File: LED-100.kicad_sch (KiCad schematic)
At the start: 98 parts, among them J2 LDA100_2_J2, J3 LDA100_2_J3, J4 LDA100_2_J4, J5 xtra, J6 Conn_01x09, J7 Conn_01x01, SW1 SW_SPDT, U1 TLC5947DAP, U2 TLC5947DAP, U3 TLC5947DAP

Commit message: cleanup
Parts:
- U4: value ~ -> TEENSY 4.0
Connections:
- net GND: now also R1.2, R2.2, R3.2; no longer R1.1, R2.1, R3.1
- net at U1.31 (IREF): now also R1.1; no longer R1.2
- net at U3.31 (IREF): now also R3.1; no longer R3.2
- net at U2.31 (IREF): now also R2.1; no longer R2.2
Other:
- moved on the sheet: J1, J2, J3, J5, J6, J7, TP1, TP2, U1, U2, U3

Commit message: use SPI instead of I2C
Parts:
- removed J6: Conn_01x09, Connector_PinHeader_2.54mm:PinHeader_1x09_P2.54mm_Vertical, symbol Connector_Generic:Conn_01x09
- added J8: Conn_01x06, Connector_PinHeader_2.54mm:PinHeader_1x06_P2.54mm_Vertical, symbol Connector_Generic:Conn_01x06
- added R4: 100k, Resistor_THT:R_Axial_DIN0204_L3.6mm_D1.6mm_P5.08mm_Horizontal, symbol Device:R_Small_US
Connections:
- net +5V: now also R4.1
- net BLANK: now also U4.17 (15), R4.2; no longer U4.10 (8)
- net at J4.7 (PD0): now also U4.10 (8); no longer U4.11 (9)
- net at J4.6 (PD1): now also U4.11 (9); no longer U4.12 (10)
- net at J4.5 (PD2): now also U4.12 (10); no longer U4.13 (11)
- net at J4.4 (PD3): now also U4.13 (11); no longer U4.14 (12)
- net SCK: now reaches U4.15 (13)
- net SCK: now also U1.3 (SCLK), U2.3 (SCLK), U3.3 (SCLK)
- net LAT: now reaches U4.16 (14)
- net LAT: now also U1.30 (XLAT), U2.30 (XLAT), U3.30 (XLAT)
- net at U4.18 (SCL1): now also J8.6 (Pin_6)
- net at U4.19 (SDA1): now also J8.5 (Pin_5)
- net at U4.23 (21): now also J8.1 (Pin_1)
- removed net LATCH: U1.30 (XLAT), U2.30 (XLAT), U3.30 (XLAT), U4.22 (20)
- removed net SCL: U1.3 (SCLK), U2.3 (SCLK), U3.3 (SCLK), U4.21 (SCL0)
- net SDA_A: no longer names the net of U4.20 (SDA0)
- net SDA_A: now also J8.4 (Pin_4); no longer U1.4 (SIN)
- net SDA_B renamed MISO_B
- net SDA_C renamed MISO_C
- new net: J8.3 (Pin_3), U4.21 (SCL0)
- new net: J8.2 (Pin_2), U4.22 (20)
- new net MISO_A: U1.4 (SIN), U4.14 (12)
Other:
- moved on the sheet: J4, TP1, TP2

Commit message: tweaks & cleanup
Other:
- company: (none) -> Duhan Power!
- title: (none) -> LED-100
- moved on the sheet: C1, C2, C3, D1, D10, D11, D12, D13, D14, D15, D16, D17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

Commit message: rev3 first draft
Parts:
- removed RV2: R_Potentiometer_US, Potentiometer_THT:Potentiometer_Bourns_3296Y_Vertical, symbol Device:R_Potentiometer_US
- added TP3, TP4: Conn_01x01, Connector_PinHeader_2.54mm:PinHeader_1x01_P2.54mm_Vertical, symbol Connector_Generic:Conn_01x01
- J8: footprint Connector_PinHeader_2.54mm:PinHeader_1x06_P2.54mm_Vertical -> Connector_PinHeader_2.54mm:PinHeader_1x07_P2.54mm_Vertical; symbol Connector_Generic:Conn_01x06 -> Connector_Generic:Conn_01x07
- RV1: footprint Potentiometer_THT:Potentiometer_Bourns_3296Y_Vertical -> Potentiometer_THT:Potentiometer_Piher_PT-10-V10_Vertical
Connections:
- net BLANK: now also TP4.1 (Pin_1)
- net LAT: now also TP3.1 (Pin_1)
- net at U4.18 (SCL1): now also J8.7 (Pin_7); no longer J8.6 (Pin_6)
- net at U4.19 (SDA1): now also J8.6 (Pin_6); no longer J8.5 (Pin_5)
- net at U4.20 (SDA0): now also J8.5 (Pin_5); no longer J8.4 (Pin_4)
- net at U4.21 (SCL0): now also J8.4 (Pin_4); no longer J8.3 (Pin_3)
- net at U4.22 (20): now also J8.3 (Pin_3); no longer J8.2 (Pin_2)
- net at U4.23 (21): now also J8.2 (Pin_2); no longer J8.1 (Pin_1)
- net FADEIN: no longer names the net of U4.24 (22)
- net FADEIN: now also J8.1 (Pin_1); no longer RV1.2
- net FADEOUT renamed FADESPEED
- net FADESPEED: now also RV1.2
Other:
- moved on the sheet: H1, H2, H3, H4

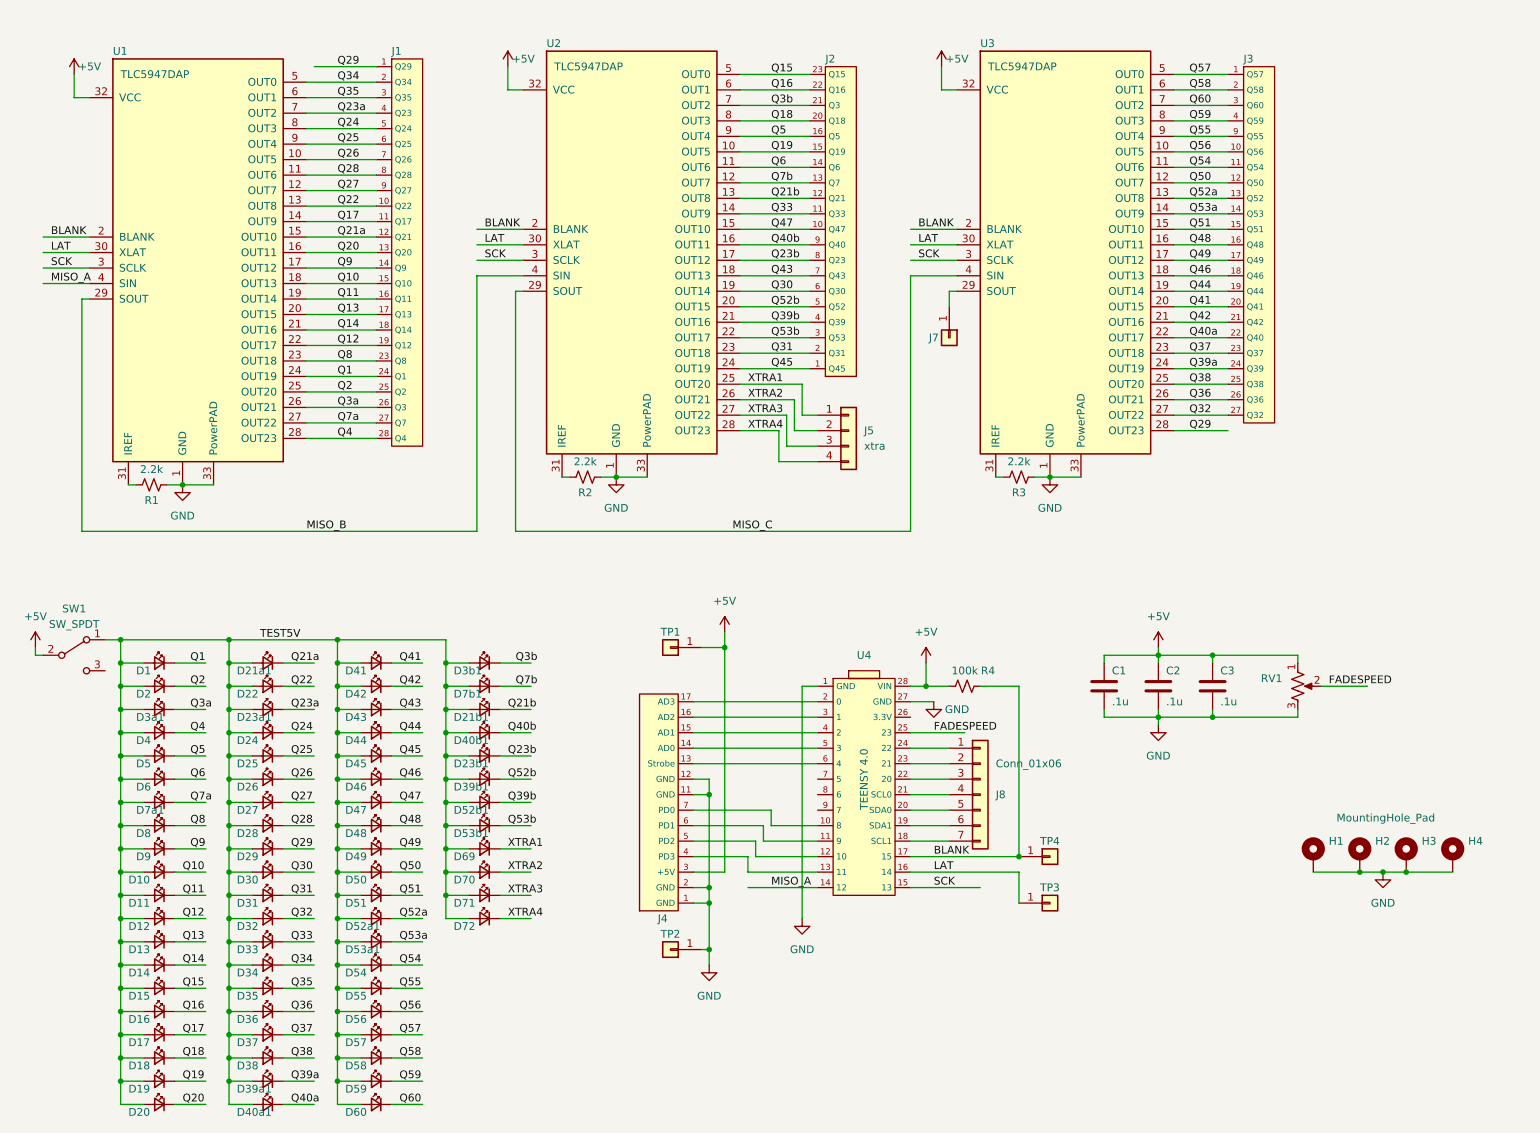
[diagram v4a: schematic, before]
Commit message: Angled teensy + updates (#1)
* diagonal teensy, pin reassignments, tweaks

* added a switch, updated to kicad 9

* rev3
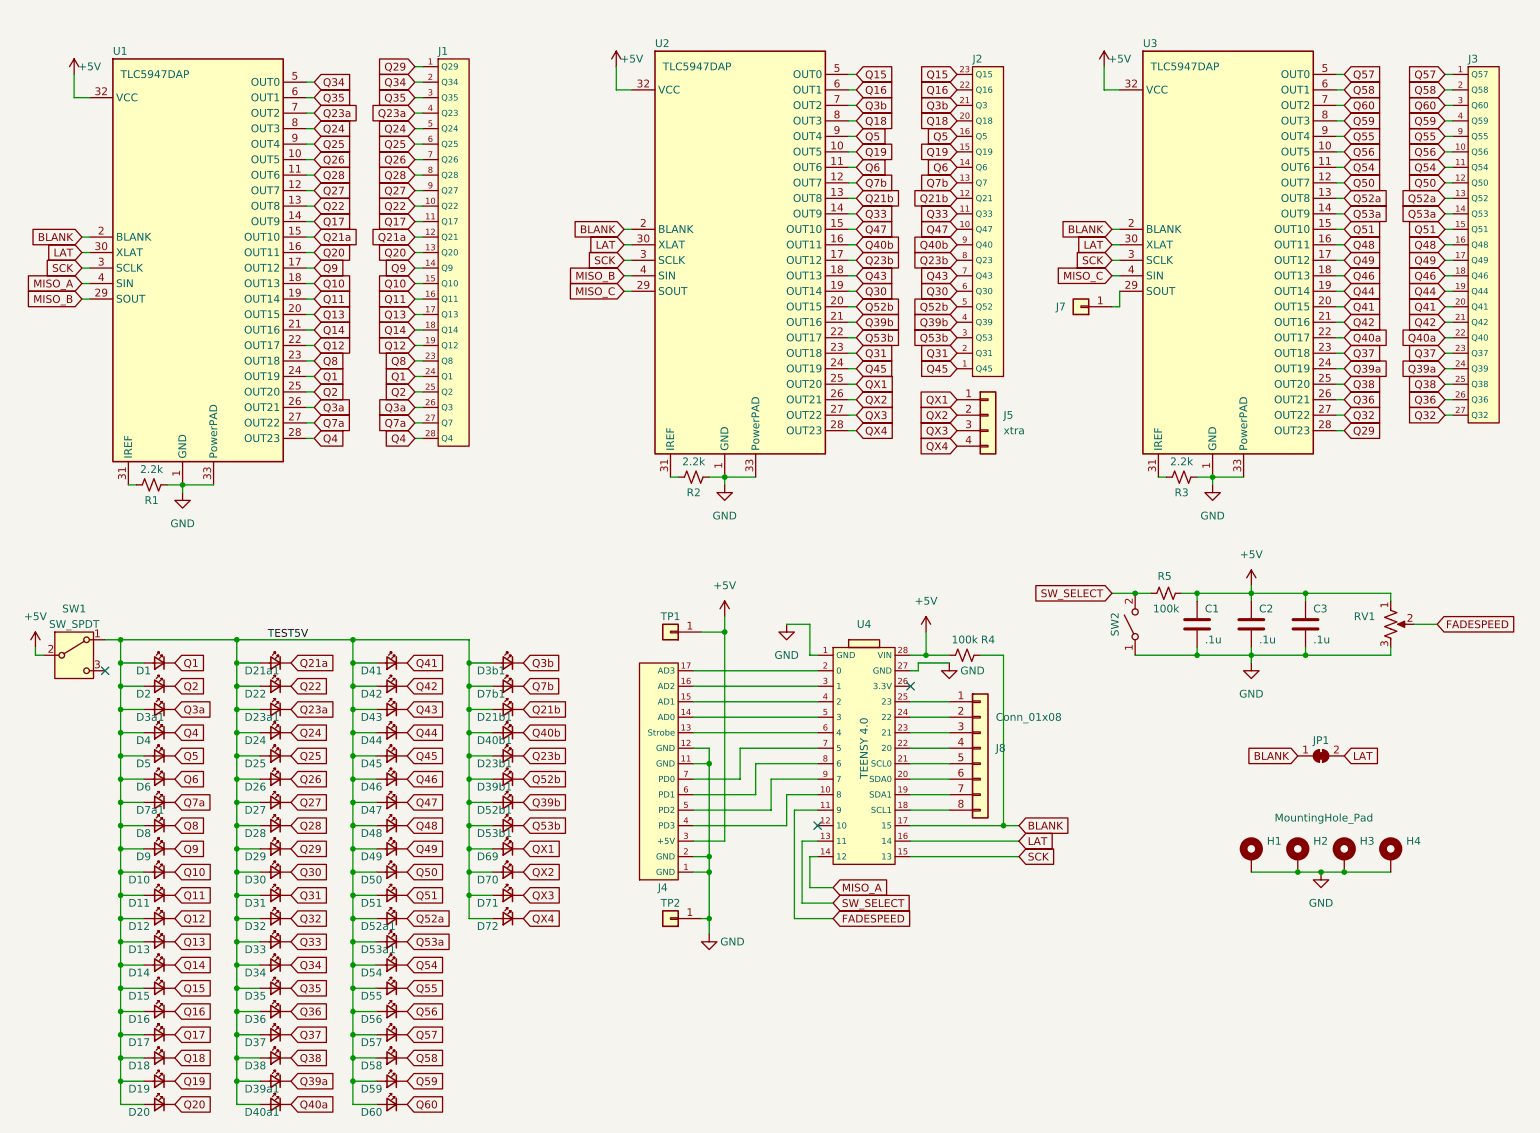
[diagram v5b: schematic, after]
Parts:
- removed TP3, TP4: Conn_01x01, Connector_PinHeader_2.54mm:PinHeader_1x01_P2.54mm_Vertical, symbol Connector_Generic:Conn_01x01
- added JP1: SolderJumper_2_Bridged, Jumper:SolderJumper-2_P1.3mm_Bridged_Pad1.0x1.5mm, symbol Jumper:SolderJumper_2_Bridged
- added R5: 100k, Resistor_THT:R_Axial_DIN0204_L3.6mm_D1.6mm_P5.08mm_Horizontal, symbol Device:R_Small_US
- added SW2: SW_SPST, Button_Switch_THT:SW_PUSH_6mm_H5mm, symbol Switch:SW_SPST
- J1: symbol F2K_Library:LDA100_2_J1 -> LED-100_Library:LDA100_2_J1
- J2: symbol F2K_Library:LDA100_2_J2 -> LED-100_Library:LDA100_2_J2
- J3: symbol F2K_Library:LDA100_2_J3 -> LED-100_Library:LDA100_2_J3
- J4: symbol F2K_Library:LDA100_2_J4 -> LED-100_Library:LDA100_2_J4
- J8: value Conn_01x06 -> Conn_01x08; footprint Connector_PinHeader_2.54mm:PinHeader_1x07_P2.54mm_Vertical -> Connector_PinHeader_2.54mm:PinHeader_1x08_P2.54mm_Vertical; symbol Connector_Generic:Conn_01x07 -> Connector_Generic:Conn_01x08
- SW1: footprint Button_Switch_THT:SW_Slide_SPDT_SLW-12689-4A-N-D -> MyParts:SWITCH_SPDT-SLW-12689-4A-N-D
- U1, U2, U3: footprint Package_SO:HTSSOP-32-1EP_6.1x11mm_P0.65mm_EP5.2x11mm_Mask4.11x4.36mm_ThermalVias -> MyParts:Package_SO_HTSSOP-32-1EP_6.1x11mm_P0.65mm_EP5.2x11mm_Mask4.11x4.36mm_ThermalVias; symbol Driver_LED:TLC5947DAP -> MySymbols:TLC5947
- U4: footprint Connector_PinHeader_2.54mm:PinHeader_2x1x14_P2.54mm_Vertical -> MyParts:Teensy 4.0; symbol F2K_Library:Teensy_4.0_headers -> LED-100_Library:Teensy_4.0_headers
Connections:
- net +5V: now also R5.1
- net BLANK: now also JP1.1 (A)
- net FADESPEED: now also U4.11 (9); no longer U4.25 (23)
- net GND: now also SW2.1 (A)
- net LAT: now also JP1.2 (B)
- net at U4.10 (8): now also J4.4 (PD3); no longer J4.7 (PD0)
- net at J4.6 (PD1): now also U4.8 (6); no longer U4.11 (9)
- net at U4.12 (10): no longer J4.5 (PD2)
- net SW_SELECT: now reaches U4.13 (11)
- net SW_SELECT: now also R5.2, SW2.2 (B); no longer J4.4 (PD3)
- net at U4.18 (SCL1): now also J8.8 (Pin_8); no longer J8.7 (Pin_7)
- net at U4.19 (SDA1): now also J8.7 (Pin_7); no longer J8.6 (Pin_6)
- net at U4.20 (SDA0): now also J8.6 (Pin_6); no longer J8.5 (Pin_5)
- net at U4.21 (SCL0): now also J8.5 (Pin_5); no longer J8.4 (Pin_4)
- net at U4.22 (20): now also J8.4 (Pin_4); no longer J8.3 (Pin_3)
- net at U4.23 (21): now also J8.3 (Pin_3); no longer J8.2 (Pin_2)
- net at U4.24 (22): now also J8.2 (Pin_2); no longer J8.1 (Pin_1)
- net at U4.7 (5): now also J4.7 (PD0)
- net at U4.9 (7): now also J4.5 (PD2)
- net XTRA1 renamed QX1
- net XTRA2 renamed QX2
- net XTRA3 renamed QX3
- net XTRA4 renamed QX4
- new net: J8.1 (Pin_1), U4.25 (23)
- no-connect marks 0 -> 3
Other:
- moved on the sheet: C1, C2, C3, D21a1, D21b1, D22, D23a1, D23b1, D24, D25, D26, D27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

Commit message: trying a wider version, WIP
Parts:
- D1, D10, D11, D12, D13, D14, D15, D16, D17, D18, D19, D2, D20, D22, D24, D25, D26, D27, D28, D29, D30, D31, D32, D33, D34, D35, D36, D37, D38, D4, D41, D42, D43, D44, D45, D46, D47, D48, D49, D5, D50, D51, D54, D55, D56, D57, D58, D59, D6, D60, D69, D70, D71, D72, D8, D9: footprint LED_SMD:LED_0805_2012Metric_Pad1.15x1.40mm_HandSolder -> LED_THT:LED_D3.0mm
- D21: renamed from D21a1; footprint LED_SMD:LED_0805_2012Metric_Pad1.15x1.40mm_HandSolder -> LED_THT:LED_D3.0mm
- D23: renamed from D23a1; footprint LED_SMD:LED_0805_2012Metric_Pad1.15x1.40mm_HandSolder -> LED_THT:LED_D3.0mm
- D3: renamed from D3a1; footprint LED_SMD:LED_0805_2012Metric_Pad1.15x1.40mm_HandSolder -> LED_THT:LED_D3.0mm
- D39: renamed from D39a1; footprint LED_SMD:LED_0805_2012Metric_Pad1.15x1.40mm_HandSolder -> LED_THT:LED_D3.0mm
- D40: renamed from D40a1; footprint LED_SMD:LED_0805_2012Metric_Pad1.15x1.40mm_HandSolder -> LED_THT:LED_D3.0mm
- D52: renamed from D52a1; footprint LED_SMD:LED_0805_2012Metric_Pad1.15x1.40mm_HandSolder -> LED_THT:LED_D3.0mm
- D53: renamed from D53a1; footprint LED_SMD:LED_0805_2012Metric_Pad1.15x1.40mm_HandSolder -> LED_THT:LED_D3.0mm
- D61: renamed from D3b1; footprint LED_SMD:LED_0805_2012Metric_Pad1.15x1.40mm_HandSolder -> LED_THT:LED_D3.0mm
- D62: renamed from D7b1; footprint LED_SMD:LED_0805_2012Metric_Pad1.15x1.40mm_HandSolder -> LED_THT:LED_D3.0mm
- D63: renamed from D21b1; footprint LED_SMD:LED_0805_2012Metric_Pad1.15x1.40mm_HandSolder -> LED_THT:LED_D3.0mm
- D64: renamed from D40b1; footprint LED_SMD:LED_0805_2012Metric_Pad1.15x1.40mm_HandSolder -> LED_THT:LED_D3.0mm
- D65: renamed from D23b1; footprint LED_SMD:LED_0805_2012Metric_Pad1.15x1.40mm_HandSolder -> LED_THT:LED_D3.0mm
- D66: renamed from D39b1; footprint LED_SMD:LED_0805_2012Metric_Pad1.15x1.40mm_HandSolder -> LED_THT:LED_D3.0mm
- D67: renamed from D52b1; footprint LED_SMD:LED_0805_2012Metric_Pad1.15x1.40mm_HandSolder -> LED_THT:LED_D3.0mm
- D68: renamed from D53b1; footprint LED_SMD:LED_0805_2012Metric_Pad1.15x1.40mm_HandSolder -> LED_THT:LED_D3.0mm
- D7: renamed from D7a1; footprint LED_SMD:LED_0805_2012Metric_Pad1.15x1.40mm_HandSolder -> LED_THT:LED_D3.0mm
- J8: value Conn_01x08 -> Conn_01x07; footprint Connector_PinHeader_2.54mm:PinHeader_1x08_P2.54mm_Vertical -> Connector_PinHeader_2.54mm:PinHeader_1x07_P2.54mm_Vertical; symbol Connector_Generic:Conn_01x08 -> Connector_Generic:Conn_01x07
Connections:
- net FADESPEED: now also U4.25 (23); no longer U4.11 (9)
- net MISO_A: now also U2.4 (SIN); no longer U1.4 (SIN)
- net MISO_B: now also U2.29 (SOUT), U3.4 (SIN); no longer U1.29 (SOUT), U2.4 (SIN)
- net MISO_C: now also U1.4 (SIN), U3.29 (SOUT); no longer U2.29 (SOUT), U3.4 (SIN)
- net at U4.18 (SCL1): now also J8.7 (Pin_7); no longer J8.8 (Pin_8)
- net at U4.19 (SDA1): now also J8.6 (Pin_6); no longer J8.7 (Pin_7)
- net at U4.20 (SDA0): now also J8.5 (Pin_5); no longer J8.6 (Pin_6)
- net at U4.21 (SCL0): now also J8.4 (Pin_4); no longer J8.5 (Pin_5)
- net at U4.22 (20): now also J8.3 (Pin_3); no longer J8.4 (Pin_4)
- net at U4.23 (21): now also J8.2 (Pin_2); no longer J8.3 (Pin_3)
- net at U4.24 (22): now also J8.1 (Pin_1); no longer J8.2 (Pin_2)
- net at J7.1 (Pin_1): now also U1.29 (SOUT); no longer U3.29 (SOUT)
- no-connect marks 3 -> 4
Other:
- moved on the sheet: D1, D10, D11, D12, D13, D14, D15, D16, D17, D18, D19, D2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

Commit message: <---wider--->
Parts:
- removed D1, D10, D11, D12, D13, D14, D15, D16, D17, D18, D19, D2, D20, D21, D22, D23, D24, D25, D26, D27, D28, D29, D3, D30, D31, D32, D33, D34, D35, D36, D37, D38, D39, D4, D40, D41, D42, D43, D44, D45, D46, D47, D48, D49, D5, D50, D51, D52, D53, D54, D55, D56, D57, D58, D59, D6, D60, D61, D62, D63, D64, D65, D66, D67, D68, D69, D7, D70, D71, D72, D8, D9: LED_Small, LED_THT:LED_D3.0mm, symbol Device:LED_Small
- removed SW1: SW_SPDT, MyParts:SWITCH_SPDT-SLW-12689-4A-N-D, symbol Switch:SW_SPDT
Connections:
- no-connect marks 4 -> 3
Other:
- moved on the sheet: C1, C2, C3, H1, H2, H3, H4, J4, J8, JP1, R4, R5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
